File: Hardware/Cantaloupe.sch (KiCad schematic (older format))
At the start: 145 parts, among them J1 OLED, J2 Interconnect, J3 ICSP, J4 BAT_CON, J5 BAT_CON_R, J6 OLED, J7 Interconnect_R, J8 ICSP_R, J9 BAT_CON_TOG, SW1 MX, SW10 MX, SW11 MX, SW12 MX, SW13 MX, SW14 MX, SW15 MX, SW16 MX, SW17 MX, SW18 MX, SW19 MX, SW2 MX, SW20 MX, SW21 MX, SW22 MX, SW23 MX, SW24 MX, SW25 MX, SW26 MX, SW27 MX, SW28 MX, SW29 MX, SW3 MX, SW30 MX, SW31 MX, SW32 MX, SW33 Encoder, SW34 MX, SW35 Reset, SW36 BAT_TOG, SW37 MX, SW38 MX, SW39 MX, SW4 MX, SW40 MX, SW41 MX, SW42 MX, SW43 MX, SW44 MX, SW45 MX, SW46 MX, SW47 MX, SW48 MX, SW49 MX, SW5 MX, SW50 MX, SW51 MX, SW52 MX, SW53 MX, SW54 MX, SW55 MX, SW56 MX, SW57 MX, SW58 MX, SW59 MX, SW6 MX, SW60 MX, SW61 MX, SW62 MX, SW63 MX, SW64 MX, SW65 MX, SW66 MX, SW67 MX, SW68 MX, SW69 Encoder_R, SW7 MX, SW70 MX, SW71 Reset, SW72 BAT_TOG_R, SW8 MX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

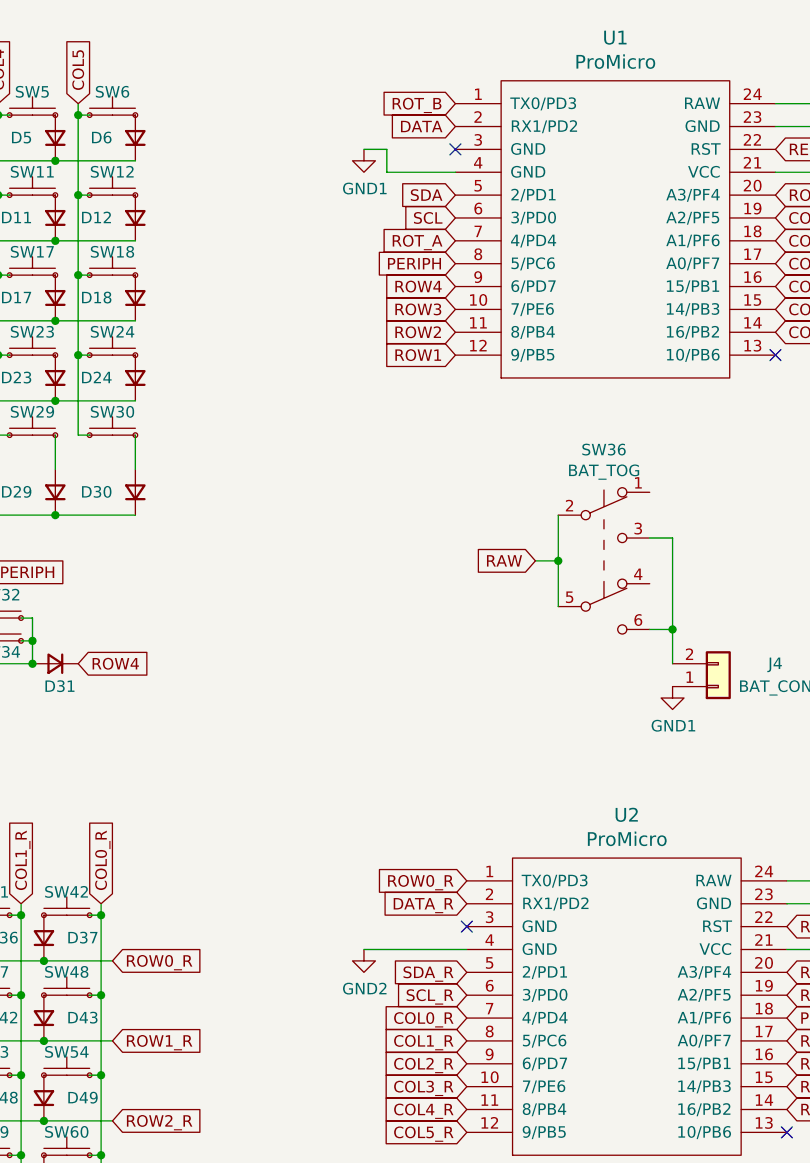
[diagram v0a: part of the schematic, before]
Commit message: Changed OLED support to 0.96" OLED
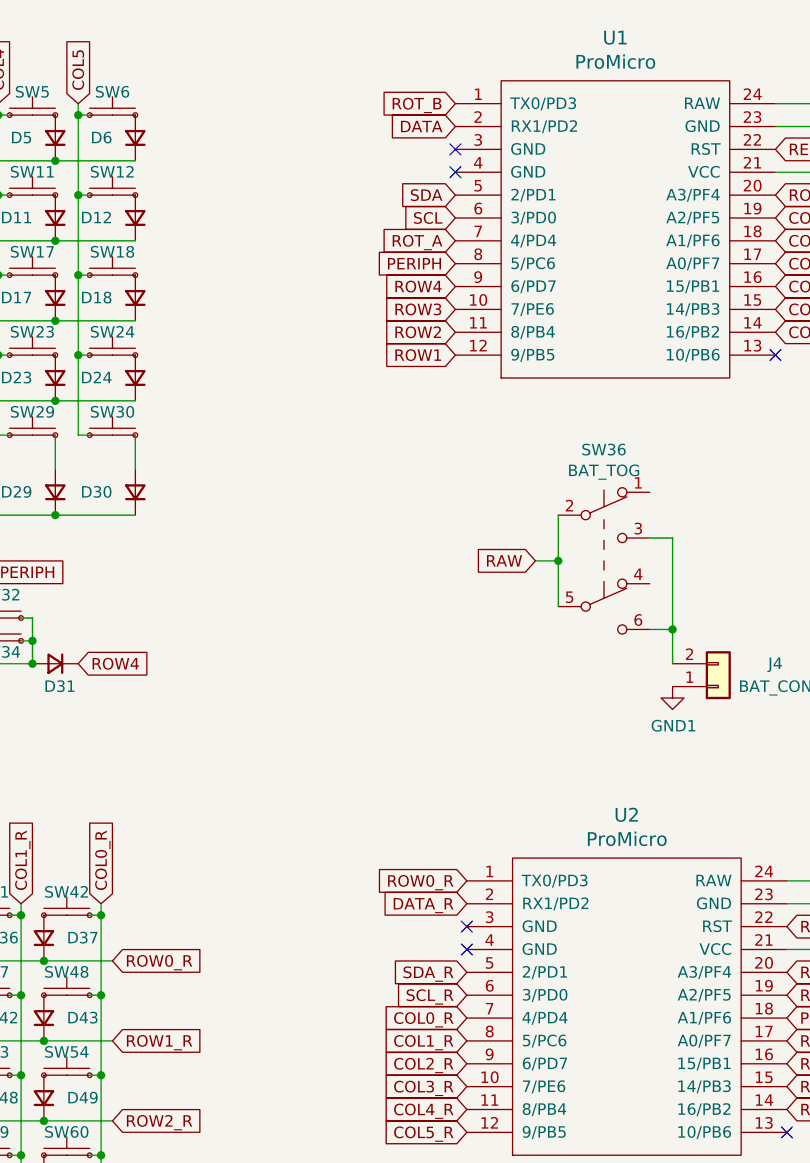
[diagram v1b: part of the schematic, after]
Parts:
- J1, J6: footprint Cantaloupe:PinHeader_1x04_P2.54mm_Vertical_No_Silk -> Cantaloupe:OLED_0.96_SSD1306_128x64
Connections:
- net GND1: no longer U1.4 (GND)
- net GND2: no longer U2.4 (GND)
- no-connect marks 12 -> 14
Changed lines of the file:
@@
 SCL
-Wire Wire Line
-	6350 1000 5850 1000
 Wire Wire Line
 	5850 1200 6150 1200
@@
 Text GLabel 5850 1400 2    50   Input ~ 0
 COL0
-Wire Wire Line
-	4450 1200 4150 1200
-Wire Wire Line
-	4150 1200 4150 1100
-Wire Wire Line
-	4150 1100 4050 1100
 NoConn ~ 5850 2000
 Wire Wire Line
@@
 Wire Wire Line
 	7700 2750 7850 2750
-$Comp
-L power:GND1 #PWR05
-U 1 1 5FB3970C
-P 4050 1100
-F 0 "#PWR05" H 4050 850 50  0001 C CNN
-F 1 "GND1" H 4055 927 50  0000 C CNN
-F 2 "" H 4050 1100 50  0001 C CNN
-F 3 "" H 4050 1100 50  0001 C CNN
-	1    4050 1100
-	1    0    0    -1
-$EndComp
 $Comp
 L power:GND1 #PWR010
@@
 $EndComp
 $Comp
-L power:GND1 #PWR04
-U 1 1 6043C4A9
-P 6350 1000
-F 0 "#PWR04" H 6350 750 50  0001 C CNN
-F 1 "GND1" H 6355 827 50  0000 C CNN
-F 2 "" H 6350 1000 50  0001 C CNN
-F 3 "" H 6350 1000 50  0001 C CNN
-	1    6350 1000
-	1    0    0    -1
-$EndComp
-$Comp
 L power:VCC #PWR03
 U 1 1 6052A13A
@@
 F 0 "J1" H 9568 625 50  0000 C CNN
 F 1 "OLED" H 9568 716 50  0000 C CNN
-F 2 "Cantaloupe:PinHeader_1x04_P2.54mm_Vertical_No_Silk" H 9650 1050 50  0001 C CNN
+F 2 "Cantaloupe:OLED_0.96_SSD1306_128x64" H 9650 1050 50  0001 C CNN
 F 3 "~" H 9650 1050 50  0001 C CNN
 	1    9650 1050
@@
 	5900 4400 6500 4400
 Wire Wire Line
-	4500 4600 4050 4600
-Wire Wire Line
 	6500 4500 6500 4400
 Connection ~ 6500 4400
@@
 F 3 "" H 9850 5200 50  0001 C CNN
 	1    9850 5200
-	1    0    0    -1
-$EndComp
-$Comp
-L power:GND2 #PWR018
-U 1 1 5FBAAC9E
-P 4050 4600
-F 0 "#PWR018" H 4050 4350 50  0001 C CNN
-F 1 "GND2" H 4055 4427 50  0000 C CNN
-F 2 "" H 4050 4600 50  0001 C CNN
-F 3 "" H 4050 4600 50  0001 C CNN
-	1    4050 4600
 	1    0    0    -1
 $EndComp
@@
 F 0 "J6" H 9768 4025 50  0000 C CNN
 F 1 "OLED" H 9768 4116 50  0000 C CNN
-F 2 "Cantaloupe:PinHeader_1x04_P2.54mm_Vertical_No_Silk" H 9850 4450 50  0001 C CNN
+F 2 "Cantaloupe:OLED_0.96_SSD1306_128x64" H 9850 4450 50  0001 C CNN
 F 3 "~" H 9850 4450 50  0001 C CNN
 	1    9850 4450
@@
 Text GLabel 2900 4400 1    50   Input ~ 0
 COL0_R
+Wire Wire Line
+	6350 1000 5850 1000
+$Comp
+L power:GND1 #PWR04
+U 1 1 6043C4A9
+P 6350 1000
+F 0 "#PWR04" H 6350 750 50  0001 C CNN
+F 1 "GND1" H 6355 827 50  0000 C CNN
+F 2 "" H 6350 1000 50  0001 C CNN
+F 3 "" H 6350 1000 50  0001 C CNN
+	1    6350 1000
+	1    0    0    -1
+$EndComp
+NoConn ~ 4450 1200
+NoConn ~ 4500 4600
 $EndSCHEMATC

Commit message: Changed orientation of 1u switches in thumb cluster. Updated plate to add 2u support.
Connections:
- net PERIPH: now also SW34.2; no longer SW34.1
- net PERIPH_R: now also SW70.2; no longer SW70.1
- net at D31.2 (A), SW32.2, SW33.S1: now also SW34.1; no longer SW34.2
- net at D62.2 (A), SW68.2, SW69.S1: now also SW70.1; no longer SW70.2
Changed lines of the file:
@@
 F 3 "~" H 2450 3450 60  0001 C CNN
 	1    2450 3250
-	-1   0    0    -1
+	1    0    0    -1
 $EndComp
 Connection ~ 2300 3150
@@
 F 3 "~" H 2350 6950 60  0001 C CNN
 	1    2350 6750
-	-1   0    0    -1
-$EndComp
-$Comp
+	1    0    0    -1
+$EndComp
+$Comp

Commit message: Updated to V1.4.
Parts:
- removed J1, J6: OLED, Cantaloupe:OLED_0.96_SSD1306_128x64, symbol Connector_Generic:Conn_01x04
- removed J3: ICSP, Connector_PinHeader_2.54mm:PinHeader_2x03_P2.54mm_Vertical, symbol Connector_Generic:Conn_02x03_Odd_Even
- removed J4: BAT_CON, Cantaloupe:Battery_Solder_Points, symbol Connector_Generic:Conn_01x02
- removed J5: BAT_CON_R, Cantaloupe:Battery_Solder_Points, symbol Connector_Generic:Conn_01x02
- removed J8: ICSP_R, Connector_PinHeader_2.54mm:PinHeader_2x03_P2.54mm_Vertical, symbol Connector_Generic:Conn_02x03_Odd_Even
- removed J9: BAT_CON_TOG, Cantaloupe:Battery_Solder_Points, symbol Connector_Generic:Conn_01x02
- removed SW36: BAT_TOG, Cantaloupe:Switch_MSK-22D18, symbol Switch:SW_Push_DPDT
- removed SW72: BAT_TOG_R, Cantaloupe:Switch_MSK-22D18, symbol Switch:SW_Push_DPDT
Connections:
- net PERIPH renamed COL6
- net PERIPH_R renamed COL6_R
- net RAW: no longer names the net of U1.24 (RAW)
- no-connect marks 14 -> 16

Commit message: Added SMK support
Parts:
- SW1, SW10, SW11, SW12, SW13, SW14, SW15, SW16, SW17, SW18, SW19, SW2, SW20, SW21, SW22, SW23, SW24, SW25, SW26, SW27, SW28, SW29, SW3, SW30, SW34, SW37, SW38, SW39, SW4, SW40, SW41, SW42, SW43, SW44, SW45, SW46, SW47, SW48, SW49, SW5, SW50, SW51, SW52, SW53, SW54, SW55, SW56, SW57, SW58, SW59, SW6, SW60, SW61, SW62, SW63, SW64, SW65, SW66, SW7, SW70, SW8, SW9: footprint Cantaloupe:HYBRID-MX_ALPS-1U-NoLED -> Cantaloupe:HYBRID-MX_ALPS_SMK-1U-NoLED
- SW31, SW32, SW67, SW68: footprint Cantaloupe:HYBRID-MX_ALPS-2U-ReversedStabilizers-NoLED -> Cantaloupe:HYBRID-MX_ALPS_SMK-2U-ReversedStabilizers-NoLED

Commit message: Updated to V1.5.
Added the option for OLED again. Removed Alps support. Improved switch footprints. Removed 2u support and moved rotary encoder positions. Deleted 61st and 62nd keyswitches - now has exactly 30 switches per side. Changed USB C interconnect back to TRRS and moved position. Unified symbol libraries
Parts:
- removed J2: Interconnect, Connector_USB:USB_C_Receptacle_HRO_TYPE-C-31-M-12, symbol Connector:USB_C_Receptacle_USB2.0
- removed J7: Interconnect_R, Connector_USB:USB_C_Receptacle_HRO_TYPE-C-31-M-12, symbol Connector:USB_C_Receptacle_USB2.0
- removed SW31, SW32, SW67, SW68: MX, Cantaloupe:HYBRID-MX_ALPS_SMK-2U-ReversedStabilizers-NoLED, symbol Cantaloupe:SW_Push_Small
- removed SW34, SW37, SW38, SW39, SW40, SW41, SW42, SW43, SW44, SW45, SW46, SW47, SW48, SW49, SW50, SW51, SW52, SW53, SW54, SW55, SW56, SW57, SW58, SW59, SW60, SW61, SW62, SW63, SW64, SW65, SW66, SW70: MX, Cantaloupe:HYBRID-MX_ALPS_SMK-1U-NoLED, symbol Cantaloupe:SW_Push_Small
- removed SW69: Encoder_R, Rotary_Encoder:RotaryEncoder_Alps_EC11E-Switch_Vertical_H20mm, symbol Device:Rotary_Encoder_Switch
- removed SW71: Reset, Button_Switch_SMD:SW_SPST_TL3342, symbol Switch:SW_Push
- removed U2: ProMicro, Cantaloupe:ArduinoProMicro_Blank, symbol Cantaloupe:ProMicro
- added J1, J3: MJ-4PP-9, Ariamelon:MJ-4PP-9_1side, symbol Ariamelon:MJ-4PP-9
- added J2: OLED_L, Ariamelon:OLED_0.96_SSD1306_128x64, symbol Connector_Generic:Conn_01x04
- added J4: OLED_R, Ariamelon:OLED_0.96_SSD1306_128x64, symbol Connector_Generic:Conn_01x04
- added SW33, SW34, SW35, SW36, SW37, SW38, SW39, SW40, SW41, SW42, SW43, SW44, SW45, SW46, SW47, SW48, SW49, SW50, SW51, SW52, SW53, SW54, SW55, SW56, SW57, SW58, SW59, SW60, SW61, SW62: MX, Ariamelon:HYBRID-MX_SMK-1U-NoLED, symbol Ariamelon:SW_Push_Small
- added SW63: Encoder, Rotary_Encoder:RotaryEncoder_Alps_EC11E-Switch_Vertical_H20mm, symbol Device:Rotary_Encoder_Switch
- added SW64: Reset, Button_Switch_SMD:SW_SPST_TL3342, symbol Switch:SW_Push
- added U2: ProMicro, Ariamelon:ArduinoProMicro_Blank, symbol Ariamelon:ProMicro
- D1, D10, D11, D12, D13, D14, D15, D16, D17, D18, D19, D2, D20, D21, D22, D23, D24, D25, D26, D27, D28, D29, D3, D30, D31, D32, D33, D34, D35, D36, D37, D38, D39, D4, D40, D41, D42, D43, D44, D45, D46, D47, D48, D49, D5, D50, D51, D52, D53, D54, D55, D56, D57, D58, D59, D6, D60, D61, D62, D7, D8, D9: footprint Cantaloupe:D_Hybrid_SOD123_DO35 -> Ariamelon:D_Hybrid_SOD123_DO35
- SW1, SW10, SW11, SW12, SW13, SW14, SW15, SW16, SW17, SW18, SW19, SW2, SW20, SW21, SW22, SW23, SW24, SW25, SW26, SW27, SW28, SW29, SW3, SW30, SW4, SW5, SW6, SW7, SW8, SW9: footprint Cantaloupe:HYBRID-MX_ALPS_SMK-1U-NoLED -> Ariamelon:HYBRID-MX_SMK-1U-NoLED; symbol Cantaloupe:SW_Push_Small -> Ariamelon:SW_Push_Small
- U1: footprint Cantaloupe:ArduinoProMicro_Blank -> Ariamelon:ArduinoProMicro_Blank; symbol Cantaloupe:ProMicro -> Ariamelon:ProMicro
- renumbered SW33 to SW31, SW35 to SW32
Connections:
- net COL0_R: now also SW38.2, SW44.2, SW50.2, SW56.2, SW62.2, U2.2 (RX1/PD2)
- net COL1_R: now also SW37.2, SW43.2, SW49.2, SW55.2, SW61.2, U2.7 (4/PD4)
- net COL2_R: now also SW36.2, SW42.2, SW48.2, SW54.2, SW60.2, U2.8 (5/PC6)
- net COL3_R: now also SW35.2, SW41.2, SW47.2, SW53.2, SW59.2, U2.9 (6/PD7)
- net COL4_R: now also SW34.2, SW40.2, SW46.2, SW52.2, SW58.2, U2.10 (7/PE6)
- net COL5_R: now also SW33.2, SW39.2, SW45.2, SW51.2, SW57.2, U2.11 (8/PB4)
- net COL6_R: now also SW63.S1, U2.19 (A2/PF5)
- net DATA_R: now also J3.D, U2.20 (A3/PF4)
- net RESET_R: now also SW64.1, U2.22 (RST)
- net ROT_A_R: now also SW63.A, U2.17 (A0/PF7)
- net ROT_B_R: now also SW63.B, U2.18 (A1/PF6)
- net ROW0_R: now also U2.1 (TX0/PD3)
- net ROW1_R: now also U2.13 (10/PB6)
- net ROW2_R: now also U2.14 (16/PB2)
- net ROW3_R: now also D62.1 (K), U2.15 (14/PB3)
- net ROW4_R: now also U2.16 (15/PB1); no longer D62.1 (K)
- net SCL_R: now also J4.3 (Pin_3), U2.6 (3/PD0)
- net SDA_R: now also J4.4 (Pin_4), U2.5 (2/PD1)
- net GND_L: now reaches U1.4 (GND)
- net GND_L: now also SW31.C, SW32.2, J1.A, J1.B, J2.1 (Pin_1)
- net at D56.2 (A): now also SW57.1
- net at D33.2 (A): now also SW34.1
- net at D39.2 (A): now also SW40.1
- net at D45.2 (A): now also SW46.1
- net at D51.2 (A): now also SW52.1
- net at D57.2 (A): now also SW58.1
- net at D37.2 (A): now also SW38.1
- net at D49.2 (A): now also SW50.1
- net at D43.2 (A): now also SW44.1
- net at D55.2 (A): now also SW56.1
- net at D61.2 (A): now also SW62.1
- net at D60.2 (A): now also SW61.1
- net at D54.2 (A): now also SW55.1
- net at D48.2 (A): now also SW49.1
- net at D42.2 (A): now also SW43.1
- net at D59.2 (A): now also SW60.1
- net at D58.2 (A): now also SW59.1
- net at D50.2 (A): now also SW51.1
- net at D44.2 (A): now also SW45.1
- net at D38.2 (A): now also SW39.1
- net at D32.2 (A): now also SW33.1
- net at D52.2 (A): now also SW53.1
- net at D46.2 (A): now also SW47.1
- net at D40.2 (A): now also SW41.1
- net at D34.2 (A): now also SW35.1
- net at D53.2 (A): now also SW54.1
- net at D47.2 (A): now also SW48.1
- net at D41.2 (A): now also SW42.1
- net at D35.2 (A): now also SW36.1
- net at D36.2 (A): now also SW37.1
- net at D62.2 (A): now also SW63.S2
- net COL0 renamed COL0_L
- net COL1 renamed COL1_L
- net COL2 renamed COL2_L
- net COL3 renamed COL3_L
- net COL4 renamed COL4_L
- net COL5 renamed COL5_L
- net COL6 renamed COL6_L
- net COL6_L: now also U1.1 (TX0/PD3); no longer U1.8 (5/PC6)
- net DATA renamed DATA_L
- net DATA_L: now also J1.D
- removed net GND1: SW31.C, SW32.2, U1.23 (GND)
- net RESET renamed RESET_L
- net ROT_A renamed ROT_A_L
- net ROT_B renamed ROT_B_L
- net ROT_B_L: now also U1.8 (5/PC6); no longer U1.1 (TX0/PD3)
- net ROW0 renamed ROW0_L
- net ROW1 renamed ROW1_L
- net ROW2 renamed ROW2_L
- net ROW3 renamed ROW3_L
- net ROW3_L: now also D31.1 (K)
- net ROW4 renamed ROW4_L
- net ROW4_L: no longer D31.1 (K)
- net SCL renamed SCL_L
- net SCL_L: now also J2.3 (Pin_3)
- net SDA renamed SDA_L
- net SDA_L: now also J2.4 (Pin_4)
- net VCC renamed VDD_L
- net VDD_L: now also J1.C, J2.2 (Pin_2)
- new net GND_R: J3.A, J3.B, J4.1 (Pin_1), SW63.C, SW64.2, U2.23 (GND)
- new net VDD_R: J3.C, J4.2 (Pin_2), U2.21 (VCC)
- no-connect marks 16 -> 8
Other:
- moved on the sheet: D25, D26, D27, D28, D29, D30, D31, SW31, SW32, U1

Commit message: New ARM variant (experimental WIP)
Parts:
- removed D32, D33, D34, D35, D36, D37, D38, D39, D40, D41, D42, D43, D44, D45, D46, D47, D48, D49, D50, D51, D52, D53, D54, D55, D56, D57, D58, D59, D60, D61, D62: D, Ariamelon:D_Hybrid_SOD123_DO35, symbol Device:D_Small
- removed J1, J3: MJ-4PP-9, Ariamelon:MJ-4PP-9_1side, symbol Ariamelon:MJ-4PP-9
- removed J4: OLED_R, Ariamelon:OLED_0.96_SSD1306_128x64, symbol Connector_Generic:Conn_01x04
- removed SW32, SW64: Reset, Button_Switch_SMD:SW_SPST_TL3342, symbol Switch:SW_Push
- removed SW33, SW34, SW35, SW36, SW37, SW38, SW39, SW40, SW41, SW42, SW43, SW44, SW45, SW46, SW47, SW48, SW49, SW50, SW51, SW52, SW53, SW54, SW55, SW56, SW57, SW58, SW59, SW60, SW61, SW62: MX, Ariamelon:HYBRID-MX_SMK-1U-NoLED, symbol Ariamelon:SW_Push_Small
- removed SW63: Encoder, Rotary_Encoder:RotaryEncoder_Alps_EC11E-Switch_Vertical_H20mm, symbol Device:Rotary_Encoder_Switch
- removed U1, U2: ProMicro, Ariamelon:ArduinoProMicro_Blank, symbol Ariamelon:ProMicro
- added A1: Art, Ariamelon:Catmelon, symbol Mechanical:MountingHole
- added C1, C11, C13, C14, C3, C8, C9: 100n, Capacitor_SMD:C_0603_1608Metric, symbol Device:C_Small
- added C10, C12: 20p, Capacitor_SMD:C_0603_1608Metric, symbol Device:C_Small
- added C2, C5, C6, C7: 10u, Capacitor_SMD:C_0603_1608Metric, symbol Device:C_Small
- added C4: 1u, Capacitor_SMD:C_0603_1608Metric, symbol Device:C_Small
- added D32: Power, Ariamelon:LED_0603_1608Metric_Flippable, symbol Device:LED_Small
- added F1: 1A, Fuse:Fuse_1206_3216Metric, symbol Device:Polyfuse_Small
- added F2: 2A, Fuse:Fuse_1206_3216Metric, symbol Device:Polyfuse_Small
- added H1, H2, H3, H4, H5, H6, H7, H8: M2, Ariamelon:MountingHole_2.2mm_M2_Pad, symbol Mechanical:MountingHole
- added J1: USB_In, Ariamelon:USB-C-C168688, symbol Ariamelon:USB_C_Receptacle_USB2.0-Connector
- added J3: Link, Ariamelon:USB-C-C168688, symbol Ariamelon:USB_C_Receptacle_USB2.0-Connector
- added J4: Debug, Ariamelon:Debug_JTAG_SWD, symbol Connector_Generic:Conn_01x06
- added J5: Trackball, Ariamelon:pimoroni_trackball_flippable, symbol Connector_Generic:Conn_01x05
- added JP1: Side_L, Jumper:SolderJumper-2_P1.3mm_Open_Pad1.0x1.5mm, symbol Jumper:SolderJumper_2_Open
- added JP2: Side_R, Jumper:SolderJumper-2_P1.3mm_Open_Pad1.0x1.5mm, symbol Jumper:SolderJumper_2_Open
- added JP3: Link-_L, Jumper:SolderJumper-2_P1.3mm_Open_Pad1.0x1.5mm, symbol Jumper:SolderJumper_2_Open
- added JP4: Link+_L, Jumper:SolderJumper-2_P1.3mm_Open_Pad1.0x1.5mm, symbol Jumper:SolderJumper_2_Open
- added JP5: Link-_R, Jumper:SolderJumper-2_P1.3mm_Open_Pad1.0x1.5mm, symbol Jumper:SolderJumper_2_Open
- added JP6: Link+_R, Jumper:SolderJumper-2_P1.3mm_Open_Pad1.0x1.5mm, symbol Jumper:SolderJumper_2_Open
- added Q1: 2N7002, Package_TO_SOT_SMD:SOT-23, symbol Transistor_FET:2N7002
- added Q2: AO3401A, Package_TO_SOT_SMD:SOT-23, symbol Transistor_FET:AO3401A
- added R1, R10, R11, R12, R16, R7, R8: 10k, Resistor_SMD:R_0603_1608Metric, symbol Device:R_Small
- added R13, R9: 100k, Resistor_SMD:R_0603_1608Metric, symbol Device:R_Small
- added R14: 200k, Resistor_SMD:R_0603_1608Metric, symbol Device:R_Small
- added R15: 2k2, Resistor_SMD:R_0603_1608Metric, symbol Device:R_Small
- added R17: 220, Resistor_SMD:R_0603_1608Metric, symbol Device:R_Small
- added R2, R3: 33, Resistor_SMD:R_0603_1608Metric, symbol Device:R_Small
- added R4: 1k5, Resistor_SMD:R_0603_1608Metric, symbol Device:R_Small
- added R5, R6: 5k1, Resistor_SMD:R_0603_1608Metric, symbol Device:R_Small
- added SW32: MX, Ariamelon:Switch_TS24CA_Flippable, symbol Ariamelon:SW_SPST_Small
- added U1: STM32F303CCTx, Package_QFP:LQFP-48_7x7mm_P0.5mm, symbol MCU_ST_STM32F3:STM32F303CCTx
- added U2, U3: SRV05-4, Package_TO_SOT_SMD:SOT-23-6, symbol Power_Protection:SRV05-4
- added U4: XC6206P332MR, Package_TO_SOT_SMD:SOT-23, symbol Regulator_Linear:XC6206PxxxMR
- added U5: LMV321, Package_TO_SOT_SMD:SOT-23-5, symbol Amplifier_Operational:LMV321
- added Y1: 8MHz, Crystal:Crystal_SMD_3225-4Pin_3.2x2.5mm, symbol Device:Crystal_GND24_Small
- D1, D10, D11, D12, D13, D14, D15, D16, D17, D18, D19, D2, D20, D21, D22, D23, D24, D25, D26, D27, D28, D29, D3, D30, D31, D4, D5, D6, D7, D8, D9: footprint Ariamelon:D_Hybrid_SOD123_DO35 -> Ariamelon:D_SOD-123
- J2: value OLED_L -> OLED; footprint Ariamelon:OLED_0.96_SSD1306_128x64 -> Ariamelon:OLED_0.96_SSD1306_128x64_Flippable
- SW1, SW10, SW11, SW12, SW13, SW14, SW15, SW16, SW17, SW18, SW19, SW2, SW20, SW21, SW22, SW23, SW24, SW25, SW26, SW27, SW28, SW29, SW3, SW30, SW4, SW5, SW6, SW7, SW8, SW9: footprint Ariamelon:HYBRID-MX_SMK-1U-NoLED -> Ariamelon:MXOnly-1U-Hotswap-Dual; symbol Ariamelon:SW_Push_Small -> Ariamelon:SW_SPST_Small
- SW31: footprint Rotary_Encoder:RotaryEncoder_Alps_EC11E-Switch_Vertical_H20mm -> Ariamelon:EC11_Flippable
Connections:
- net COL6_L is gone; now on an unnamed net: SW31.S2
- net at D30.2 (A): now also SW30.1 (A); no longer SW30.2
- net at D31.2 (A): no longer SW31.S1
- net COL0_L renamed COL0
- net COL0: now also U1.28 (PB15)
- net COL1_L renamed COL1
- net COL1: now also U1.27 (PB14)
- net COL2_L renamed COL2
- net COL2: now also U1.26 (PB13)
- net COL3_L renamed COL3
- net COL3: now also U1.25 (PB12)
- net COL4_L renamed COL4
- net COL4: now also U1.20 (PB2)
- net COL5_L renamed COL5
- net COL5: now also SW30.2 (B), U1.19 (PB1); no longer SW30.1
- net GND_L renamed GND
- net GND: now also C1.1, C10.1, C11.1, C12.1, C13.1, C14.1, C3.1, C4.1, C5.1, C6.1, C7.1, C8.1, C9.1, J1.A1 (GND), J1.A12 (GND), J1.B1 (GND), J1.B12 (GND), J1.S1 (SHIELD), J3.A1 (GND), J3.A12 (GND), J3.B1 (GND), J3.B12 (GND), J3.S1 (SHIELD), J4.1 (Pin_1), J5.5 (Pin_5), JP2.1 (A), Q1.2 (S), R14.2, R15.2, R5.1, R6.1, R7.2, R9.2, U1.23 (VSS), U1.35 (VSS), U1.47 (VSS), U1.8 (VSSA), U2.2 (VN), U3.2 (VN), U4.1 (GND), U5.2 (V-), Y1.2, Y1.4
- net ROT_A_L: no longer names the net of SW31.A
- net ROT_A_L: now also C1.2, R1.2, R8.1
- net ROT_B_L: no longer names the net of SW31.B
- net ROT_B_L: now also C3.2, R10.2, R12.1
- net ROW0_L renamed ROW0
- net ROW0: now also U1.30 (PA9)
- net ROW1_L renamed ROW1
- net ROW1: now also U1.29 (PA8)
- net ROW2_L renamed ROW2
- net ROW2: now also U1.18 (PB0)
- net ROW3_L renamed ROW3
- net ROW3: now also U1.17 (PA7)
- net ROW4_L renamed ROW4
- net ROW4: now also U1.16 (PA6)
- net SCL_L renamed SCL
- net SCL: now also J5.3 (Pin_3), U1.42 (PB6)
- net SDA_L renamed SDA
- net SDA: now also J5.2 (Pin_2), U1.43 (PB7)
- net VDD_L renamed VDD
- net VDD: now also C11.2, C13.2, C14.2, C7.2, C8.2, C9.2, D32.2 (A), J4.6 (Pin_6), J5.1 (Pin_1), JP1.1 (A), R10.1, R11.1, R4.1, R8.2, SW32.2 (B), U1.1 (VBAT), U1.24 (VDD), U1.36 (VDD), U1.48 (VDD), U1.9 (VDDA), U4.2 (VO)
- new net: J1.A5 (CC1), R5.2
- new net: J1.B5 (CC2), R6.2
- new net: R2.2, U1.32 (PA11)
- new net: R3.2, U1.33 (PA12)
- new net: JP1.2 (B), JP2.2 (B), R16.2
- new net: C2.1, Q1.1 (G), R9.1
- new net: F2.1, Q2.3 (D), R13.1, U5.3 (-)
- new net: Q2.1 (G), U5.4
- new net: D32.1 (K), R15.1
- new net: C12.2, R17.2, Y1.3
- new net BOOT0: C2.2, R7.1, SW32.1 (A), U1.44 (BOOT0)
- new net COLROT: SW31.S1, U1.15 (PA5)
- new net D+: J1.A6 (D+), J1.B6 (D+), R3.1, R4.2, U2.3 (IO2)
- new net D-: J1.A7 (D-), J1.B7 (D-), R2.1, U2.1 (IO1)
- new net HSE_IN: C10.2, U1.5 (PF0), Y1.1
- new net HSE_OUT: R17.1, U1.6 (PF1)
- new net JTCK: J4.4 (Pin_4), U1.37 (PA14)
- new net JTD0: J4.3 (Pin_3), U1.39 (PB3)
- new net JTDI: J4.2 (Pin_2), U1.38 (PA15)
- new net JTMS: J4.5 (Pin_5), U1.34 (PA13)
- new net Link+: J3.A6 (D+), J3.B6 (D+), JP4.2 (B), JP6.2 (B), U3.3 (IO2)
- new net Link-: J3.A7 (D-), J3.B7 (D-), JP3.2 (B), JP5.2 (B), U3.1 (IO1)
- new net NRST: C4.2, Q1.3 (D), R11.2, U1.7 (NRST)
- new net PLUGGED: R13.2, R14.1, U1.31 (PA10)
- new net ROT_A: R1.1, U1.41 (PB5)
- new net ROT_B: R12.2, U1.14 (PA4)
- new net RX: JP3.1 (A), JP6.1 (A), U1.22 (PB11)
- new net Side: R16.1, U1.2 (PC13)
- new net TX: JP4.1 (A), JP5.1 (A), U1.21 (PB10)
- new net VBUS: F2.2, J1.A4 (VBUS), J1.A9 (VBUS), J1.B4 (VBUS), J1.B9 (VBUS), U2.5 (VP)
- new net VBUS_In: C6.2, F1.2, Q2.2 (S), U4.3 (VI), U5.1 (+), U5.5 (V+)
- new net VBUS_In_Fused: C5.2, F1.1, J3.A4 (VBUS), J3.A9 (VBUS), J3.B4 (VBUS), J3.B9 (VBUS), U3.5 (VP)
- no-connect marks 8 -> 11
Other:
- note added: "Digital Power"
- note added: "ESD protection"
- note added: "Encoder"
- note added: "Fuse/Plug detect"
- note added: "HSE Clock"
- note added: "JTAG/SWD"
- note added: "MCU"
- note added: "Matrix"
- note added: "OLED"
- note added: "Reset/DFU Bootloader"
- note added: "Side detection"
- note added: "Split connect"
- note added: "Trackball"
- note added: "USB"
- moved on the sheet: D1, D10, D11, D12, D13, D14, D15, D16, D17, D18, D19, D2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
